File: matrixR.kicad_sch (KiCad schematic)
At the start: 68 parts, among them SW34 SW_Push, SW35 SW_Push, SW36 SW_Push, SW37 SW_Push, SW38 SW_Push, SW39 SW_Push, SW40 SW_Push, SW41 SW_Push, SW42 SW_Push, SW43 SW_Push, SW44 SW_Push, SW45 SW_Push, SW46 SW_Push, SW47 SW_Push, SW48 SW_Push, SW49 SW_Push, SW50 SW_Push, SW51 SW_Push, SW52 SW_Push, SW53 SW_Push, SW54 SW_Push, SW55 SW_Push, SW56 SW_Push, SW57 SW_Push, SW58 SW_Push, SW59 SW_Push, SW60 SW_Push, SW61 SW_Push, SW62 SW_Push, SW63 SW_Push, SW64 SW_Push, SW65 SW_Push, SW66 SW_Push, SW67 SW_Push

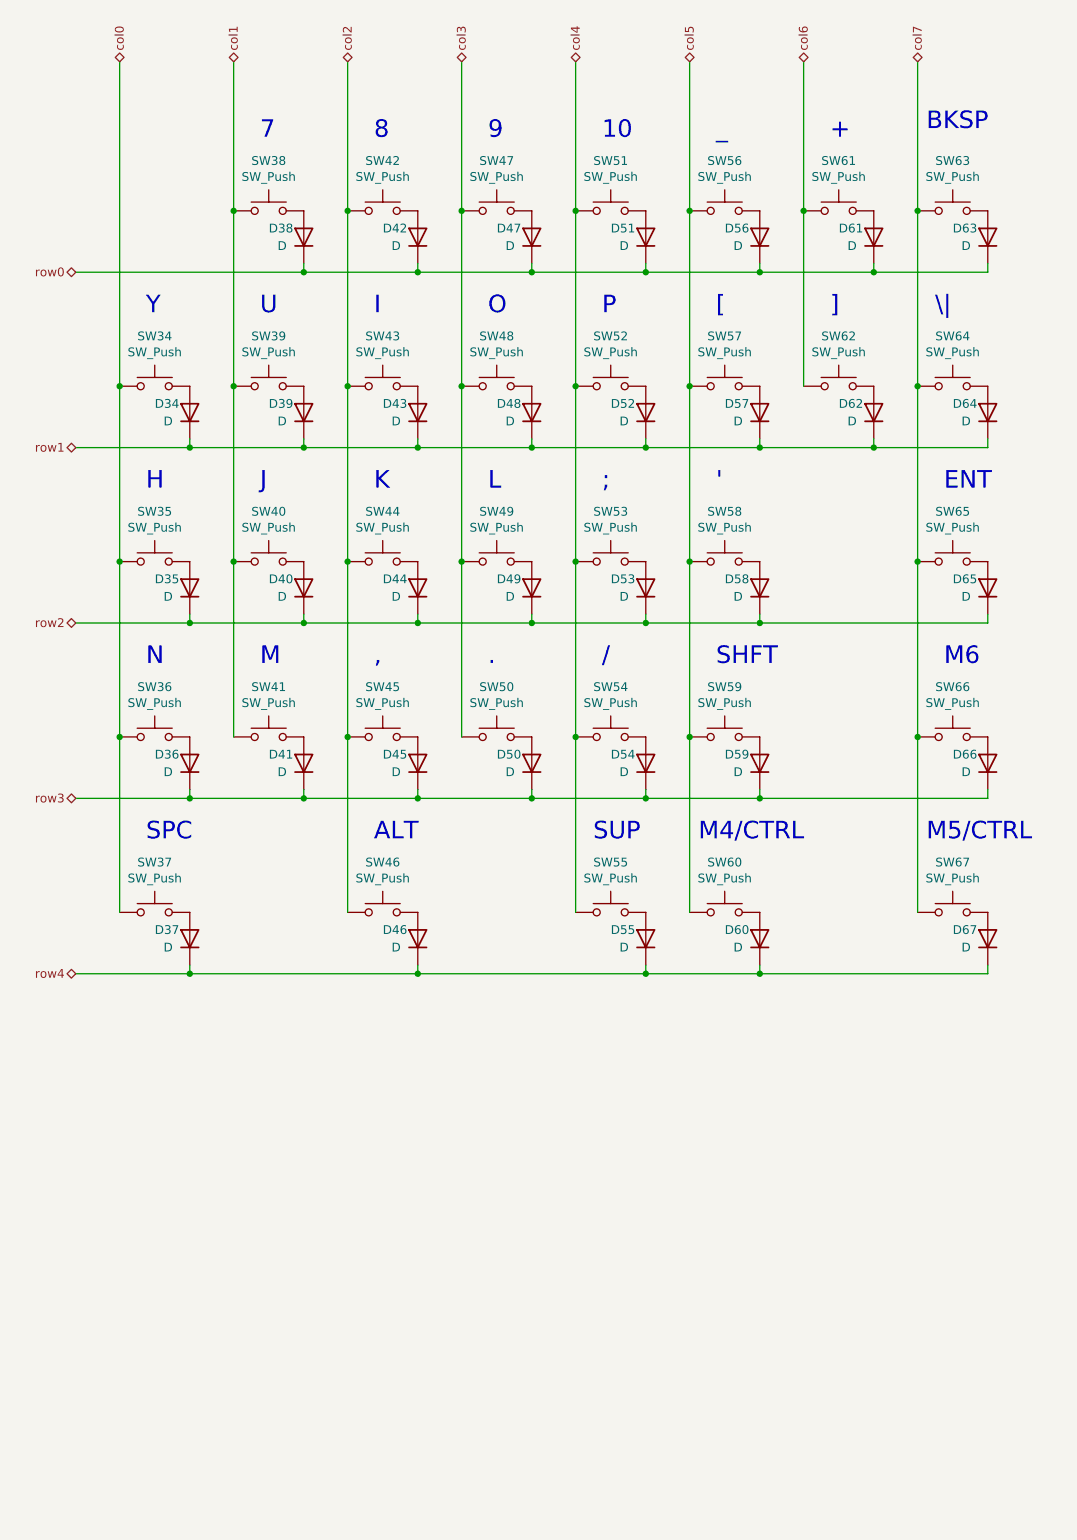
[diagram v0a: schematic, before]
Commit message: Hot pluggable trrs
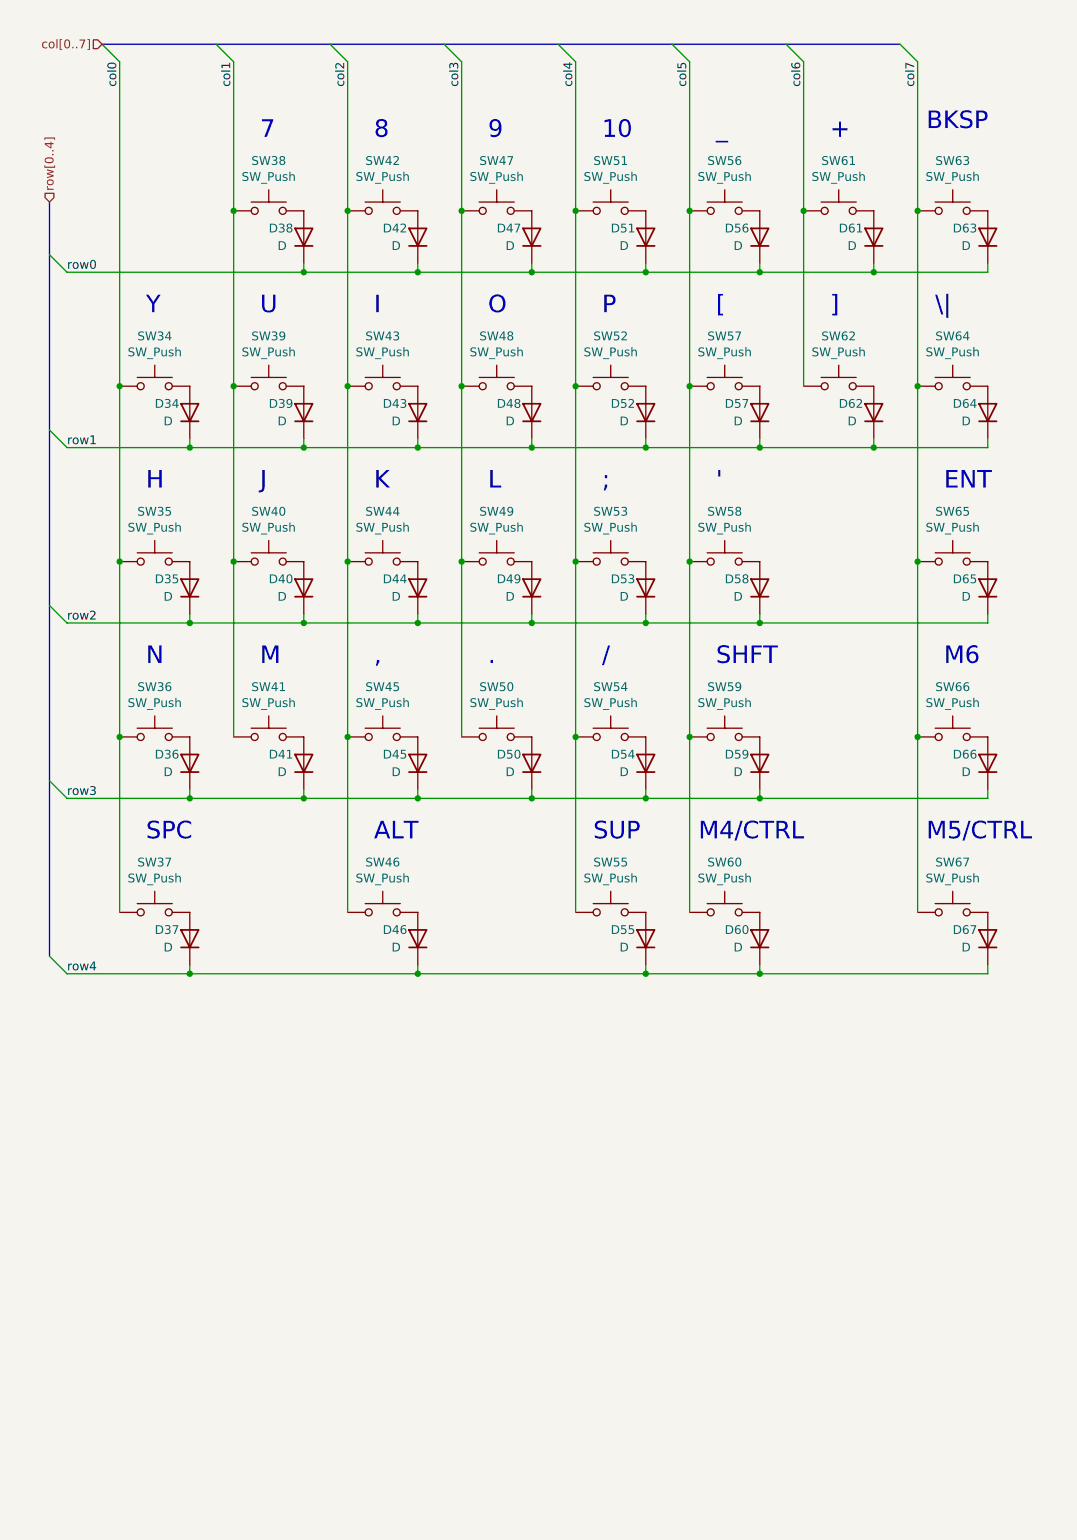
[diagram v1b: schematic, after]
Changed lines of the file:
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@@
   (junction (at 76.2 96.52) (diameter 0) (color 0 0 0 0)
   )
+  (junction (at 59.69 45.72) (diameter 0) (color 0 0 0 0)
+  )
+  (junction (at 59.69 71.12) (diameter 0) (color 0 0 0 0)
+  )
+  (junction (at 26.67 121.92) (diameter 0) (color 0 0 0 0)
+  )
   (junction (at 36.83 156.21) (diameter 0) (color 0 0 0 0)
   )
-  (junction (at 59.69 45.72) (diameter 0) (color 0 0 0 0)
-  )
-  (junction (at 59.69 71.12) (diameter 0) (color 0 0 0 0)
-  )
-  (junction (at 26.67 121.92) (diameter 0) (color 0 0 0 0)
-  )
   (junction (at 125.73 45.72) (diameter 0) (color 0 0 0 0)
   )
@@
   (junction (at 26.67 96.52) (diameter 0) (color 0 0 0 0)
   )
+  (bus_entry (at 16.51 128.27) (size 2.54 2.54)
+    (stroke (width 0) (type default) (color 0 0 0 0))
+  )
+  (bus_entry (at 16.51 52.07) (size 2.54 2.54)
+    (stroke (width 0) (type default) (color 0 0 0 0))
+  )
+  (bus_entry (at 16.51 102.87) (size 2.54 2.54)
+    (stroke (width 0) (type default) (color 0 0 0 0))
+  )
+  (bus_entry (at 139.7 21.59) (size 2.54 2.54)
+    (stroke (width 0) (type default) (color 0 0 0 0))
+  )
+  (bus_entry (at 123.19 21.59) (size 2.54 2.54)
+    (stroke (width 0) (type default) (color 0 0 0 0))
+  )
+  (bus_entry (at 90.17 21.59) (size 2.54 2.54)
+    (stroke (width 0) (type default) (color 0 0 0 0))
+  )
+  (bus_entry (at 106.68 21.59) (size 2.54 2.54)
+    (stroke (width 0) (type default) (color 0 0 0 0))
+  )
+  (bus_entry (at 73.66 21.59) (size 2.54 2.54)
+    (stroke (width 0) (type default) (color 0 0 0 0))
+  )
+  (bus_entry (at 24.13 21.59) (size 2.54 2.54)
+    (stroke (width 0) (type default) (color 0 0 0 0))
+  )
+  (bus_entry (at 57.15 21.59) (size 2.54 2.54)
+    (stroke (width 0) (type default) (color 0 0 0 0))
+  )
+  (bus_entry (at 40.64 21.59) (size 2.54 2.54)
+    (stroke (width 0) (type default) (color 0 0 0 0))
+  )
+  (bus_entry (at 16.51 153.67) (size 2.54 2.54)
+    (stroke (width 0) (type default) (color 0 0 0 0))
+  )
+  (bus_entry (at 16.51 77.47) (size 2.54 2.54)
+    (stroke (width 0) (type default) (color 0 0 0 0))
+  )
   (wire (pts (xy 109.22 45.72) (xy 109.22 71.12))
     (stroke (width 0) (type default) (color 0 0 0 0))
   )
-  (wire (pts (xy 20.32 54.61) (xy 53.34 54.61))
+  (wire (pts (xy 19.05 54.61) (xy 53.34 54.61))
     (stroke (width 0) (type default) (color 0 0 0 0))
   )
@@
     (stroke (width 0) (type default) (color 0 0 0 0))
   )
+  (bus (pts (xy 123.19 21.59) (xy 139.7 21.59))
+    (stroke (width 0) (type default) (color 0 0 0 0))
+  )
   (wire (pts (xy 53.34 129.54) (xy 53.34 130.81))
     (stroke (width 0) (type default) (color 0 0 0 0))
@@
     (stroke (width 0) (type default) (color 0 0 0 0))
   )
-  (wire (pts (xy 20.32 130.81) (xy 36.83 130.81))
-    (stroke (width 0) (type default) (color 0 0 0 0))
-  )
   (wire (pts (xy 92.71 71.12) (xy 92.71 96.52))
     (stroke (width 0) (type default) (color 0 0 0 0))
@@
     (stroke (width 0) (type default) (color 0 0 0 0))
   )
+  (bus (pts (xy 16.51 102.87) (xy 16.51 128.27))
+    (stroke (width 0) (type default) (color 0 0 0 0))
+  )
   (wire (pts (xy 36.83 156.21) (xy 69.85 156.21))
     (stroke (width 0) (type default) (color 0 0 0 0))
   )
-  (wire (pts (xy 20.32 156.21) (xy 36.83 156.21))
-    (stroke (width 0) (type default) (color 0 0 0 0))
-  )
   (wire (pts (xy 86.36 129.54) (xy 86.36 130.81))
     (stroke (width 0) (type default) (color 0 0 0 0))
@@
     (stroke (width 0) (type default) (color 0 0 0 0))
   )
+  (bus (pts (xy 106.68 21.59) (xy 123.19 21.59))
+    (stroke (width 0) (type default) (color 0 0 0 0))
+  )
   (wire (pts (xy 119.38 154.94) (xy 119.38 156.21))
     (stroke (width 0) (type default) (color 0 0 0 0))
@@
     (stroke (width 0) (type default) (color 0 0 0 0))
   )
+  (bus (pts (xy 16.51 44.45) (xy 16.51 52.07))
+    (stroke (width 0) (type default) (color 0 0 0 0))
+  )
   (wire (pts (xy 26.67 24.13) (xy 26.67 71.12))
     (stroke (width 0) (type default) (color 0 0 0 0))
   )
+  (wire (pts (xy 19.05 130.81) (xy 36.83 130.81))
+    (stroke (width 0) (type default) (color 0 0 0 0))
+  )
   (wire (pts (xy 43.18 24.13) (xy 43.18 45.72))
     (stroke (width 0) (type default) (color 0 0 0 0))
   )
+  (bus (pts (xy 57.15 21.59) (xy 73.66 21.59))
+    (stroke (width 0) (type default) (color 0 0 0 0))
+  )
+  (bus (pts (xy 16.51 52.07) (xy 16.51 77.47))
+    (stroke (width 0) (type default) (color 0 0 0 0))
+  )
   (wire (pts (xy 86.36 78.74) (xy 86.36 80.01))
     (stroke (width 0) (type default) (color 0 0 0 0))
@@
     (stroke (width 0) (type default) (color 0 0 0 0))
   )
+  (bus (pts (xy 16.51 77.47) (xy 16.51 102.87))
+    (stroke (width 0) (type default) (color 0 0 0 0))
+  )
   (wire (pts (xy 109.22 24.13) (xy 109.22 45.72))
     (stroke (width 0) (type default) (color 0 0 0 0))
@@
     (stroke (width 0) (type default) (color 0 0 0 0))
   )
+  (bus (pts (xy 73.66 21.59) (xy 90.17 21.59))
+    (stroke (width 0) (type default) (color 0 0 0 0))
+  )
+  (bus (pts (xy 40.64 21.59) (xy 57.15 21.59))
+    (stroke (width 0) (type default) (color 0 0 0 0))
+  )
   (wire (pts (xy 119.38 105.41) (xy 152.4 105.41))
     (stroke (width 0) (type default) (color 0 0 0 0))
@@
     (stroke (width 0) (type default) (color 0 0 0 0))
   )
-  (wire (pts (xy 20.32 105.41) (xy 36.83 105.41))
+  (wire (pts (xy 19.05 105.41) (xy 36.83 105.41))
     (stroke (width 0) (type default) (color 0 0 0 0))
   )
@@
     (stroke (width 0) (type default) (color 0 0 0 0))
   )
+  (bus (pts (xy 90.17 21.59) (xy 106.68 21.59))
+    (stroke (width 0) (type default) (color 0 0 0 0))
+  )
+  (wire (pts (xy 19.05 156.21) (xy 36.83 156.21))
+    (stroke (width 0) (type default) (color 0 0 0 0))
+  )
   (wire (pts (xy 86.36 130.81) (xy 102.87 130.81))
     (stroke (width 0) (type default) (color 0 0 0 0))
@@
     (stroke (width 0) (type default) (color 0 0 0 0))
   )
+  (bus (pts (xy 16.51 128.27) (xy 16.51 153.67))
+    (stroke (width 0) (type default) (color 0 0 0 0))
+  )
   (wire (pts (xy 152.4 53.34) (xy 152.4 54.61))
     (stroke (width 0) (type default) (color 0 0 0 0))
@@
     (stroke (width 0) (type default) (color 0 0 0 0))
   )
+  (bus (pts (xy 24.13 21.59) (xy 40.64 21.59))
+    (stroke (width 0) (type default) (color 0 0 0 0))
+  )
   (wire (pts (xy 92.71 121.92) (xy 92.71 147.32))
     (stroke (width 0) (type default) (color 0 0 0 0))
@@
     (stroke (width 0) (type default) (color 0 0 0 0))
   )
-  (wire (pts (xy 20.32 80.01) (xy 36.83 80.01))
+  (wire (pts (xy 19.05 80.01) (xy 36.83 80.01))
     (stroke (width 0) (type default) (color 0 0 0 0))
   )
@@
     (effects (font (size 2.54 2.54)) (justify left bottom))
   )
-  (hierarchical_label "col1" (shape tri_state) (at 43.18 24.13 90)
+  (label "col1" (at 43.18 24.13 270)
+    (effects (font (size 1.27 1.27)) (justify right bottom))
+  )
+  (label "col5" (at 109.22 24.13 270)
+    (effects (font (size 1.27 1.27)) (justify right bottom))
+  )
+  (label "col6" (at 125.73 24.13 270)
+    (effects (font (size 1.27 1.27)) (justify right bottom))
+  )
+  (label "col4" (at 92.71 24.13 270)
+    (effects (font (size 1.27 1.27)) (justify right bottom))
+  )
+  (label "col7" (at 142.24 24.13 270)
+    (effects (font (size 1.27 1.27)) (justify right bottom))
+  )
+  (label "row1" (at 19.05 80.01 0)
+    (effects (font (size 1.27 1.27)) (justify left bottom))
+  )
+  (label "row4" (at 19.05 156.21 0)
+    (effects (font (size 1.27 1.27)) (justify left bottom))
+  )
+  (label "col2" (at 59.69 24.13 270)
+    (effects (font (size 1.27 1.27)) (justify right bottom))
+  )
+  (label "col0" (at 26.67 24.13 270)
+    (effects (font (size 1.27 1.27)) (justify right bottom))
+  )
+  (label "row0" (at 19.05 54.61 0)
+    (effects (font (size 1.27 1.27)) (justify left bottom))
+  )
+  (label "row3" (at 19.05 130.81 0)
+    (effects (font (size 1.27 1.27)) (justify left bottom))
+  )
+  (label "col3" (at 76.2 24.13 270)
+    (effects (font (size 1.27 1.27)) (justify right bottom))
+  )
+  (label "row2" (at 19.05 105.41 0)
+    (effects (font (size 1.27 1.27)) (justify left bottom))
+  )
+  (hierarchical_label "row[0..4]" (shape input) (at 16.51 44.45 90)
     (effects (font (size 1.27 1.27)) (justify left))
   )
-  (hierarchical_label "col7" (shape tri_state) (at 142.24 24.13 90)
-    (effects (font (size 1.27 1.27)) (justify left))
-  )
-  (hierarchical_label "row1" (shape tri_state) (at 20.32 80.01 180)
+  (hierarchical_label "col[0..7]" (shape input) (at 24.13 21.59 180)
     (effects (font (size 1.27 1.27)) (justify right))
   )
-  (hierarchical_label "col2" (shape tri_state) (at 59.69 24.13 90)
-    (effects (font (size 1.27 1.27)) (justify left))
-  )
-  (hierarchical_label "col0" (shape tri_state) (at 26.67 24.13 90)
-    (effects (font (size 1.27 1.27)) (justify left))
-  )
-  (hierarchical_label "row2" (shape tri_state) (at 20.32 105.41 180)
-    (effects (font (size 1.27 1.27)) (justify right))
-  )
-  (hierarchical_label "row0" (shape tri_state) (at 20.32 54.61 180)
-    (effects (font (size 1.27 1.27)) (justify right))
-  )
-  (hierarchical_label "col5" (shape tri_state) (at 109.22 24.13 90)
-    (effects (font (size 1.27 1.27)) (justify left))
-  )
-  (hierarchical_label "row4" (shape tri_state) (at 20.32 156.21 180)
-    (effects (font (size 1.27 1.27)) (justify right))
-  )
-  (hierarchical_label "row3" (shape tri_state) (at 20.32 130.81 180)
-    (effects (font (size 1.27 1.27)) (justify right))
-  )
-  (hierarchical_label "col6" (shape tri_state) (at 125.73 24.13 90)
-    (effects (font (size 1.27 1.27)) (justify left))
-  )
-  (hierarchical_label "col4" (shape tri_state) (at 92.71 24.13 90)
-    (effects (font (size 1.27 1.27)) (justify left))
-  )
-  (hierarchical_label "col3" (shape tri_state) (at 76.2 24.13 90)
-    (effects (font (size 1.27 1.27)) (justify left))
-  )
   (symbol (lib_id "Device:D") (at 86.36 49.53 90) (unit 1)

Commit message: No more erc errors + centering and socketing of switches
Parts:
- SW34, SW35, SW36, SW38, SW39, SW40, SW41, SW42, SW43, SW44, SW45, SW47, SW48, SW49, SW50, SW51, SW52, SW53, SW54, SW56, SW57, SW58, SW61, SW62, SW66, SW67: footprint MX_Switch:SW_Cherry_MX_1.00u_PCB -> MX_Switch:SW_Cherry_MX_1.00u_PCB_Socket
- SW37: footprint MX_Switch:SW_Cherry_MX_2.75u_PCB_ReversedStabilizers -> MX_Switch:SW_Cherry_MX_2.75u_PCB_Socket_ReversedStabilizers
- SW46, SW55, SW60, SW64: footprint MX_Switch:SW_Cherry_MX_1.50u_PCB -> MX_Switch:SW_Cherry_MX_1.50u_PCB_Socket
- SW59: footprint MX_Switch:SW_Cherry_MX_2.00u_PCB_ReversedStabilizers -> MX_Switch:SW_Cherry_MX_2.00u_PCB_Socket_ReversedStabilizers
- SW63: footprint MX_Switch:SW_Cherry_MX_2.00u_PCB -> MX_Switch:SW_Cherry_MX_2.00u_PCB_Socket
- SW65: footprint MX_Switch:SW_Cherry_MX_2.25u_PCB_ReversedStabilizers -> MX_Switch:SW_Cherry_MX_2.25u_PCB_Socket_ReversedStabilizers
